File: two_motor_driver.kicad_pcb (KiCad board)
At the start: 4 copper layers, 123.8 x 60 mm, 51 parts, among them M1 Conn_01x03, M2 Conn_01x03, SW1 SW_SPDT, U1 L6234PD, U2 L6234PD, U3 INA181, U4 INA181, U5 my_buck_boost

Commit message: pcb layout
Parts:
- removed .033_1, .033_2: .033, Resistor_SMD:R_1206_3216Metric
- removed .1_1, .1_2: .1, Resistor_SMD:R_1206_3216Metric
- removed .22uF_1, .22uF_2: .22uF, Capacitor_SMD:C_0805_2012Metric
- removed 100nF_1, 100nF_2, C11, C12, C13, C14, C15, C16: 100nF, Capacitor_SMD:C_0805_2012Metric
- removed 100uF_1, 100uF_2: 100uF, Capacitor_SMD:C_1210_3225Metric
- removed 10nF_1, 10nF_2: 10nF, Capacitor_SMD:C_0805_2012Metric
- removed 1uF_1, 1uF_2: 1uF, Capacitor_SMD:C_0805_2012Metric
- removed 90k_1: 90k, Resistor_SMD:R_0805_2012Metric
- removed BJ1: Barrel_Jack, Connector_BarrelJack:BarrelJack_CUI_PJ-063AH_Horizontal
- removed D2, D3: BAT54S, Package_TO_SOT_SMD:SOT-23-3
- removed JP1, JP3, JP4, JP5: SolderJumper_2_Open, Jumper:SolderJumper-2_P1.3mm_Open_TrianglePad1.0x1.5mm
- removed M1, M2, PIR1: Conn_01x03, Connector_PinHeader_2.54mm:PinHeader_1x03_P2.54mm_Vertical
- removed U1, U2: L6234PD, SOIC127P1420X360-21N
- removed U3, U4: INA181, Package_TO_SOT_SMD:SOT-23-6
- added 10k_2: 10k, Resistor_SMD:R_0805_2012Metric, F.Cu at (197.0, 120.4)
- added 90k_2: 90k, Resistor_SMD:R_0805_2012Metric, F.Cu at (197.0, 124.9)
- added C1: 100nF, Capacitor_SMD:C_0805_2012Metric, F.Cu at (198.9, 147.9)
- added C2: 100nF, Capacitor_SMD:C_0805_2012Metric, F.Cu at (201.9, 147.9)
- added FOC1: Conn_01x05, Connector_PinSocket_2.54mm:PinSocket_1x05_P2.54mm_Vertical, F.Cu at (193.4, 95.5)
- added FOC2: Conn_01x05, Connector_PinSocket_2.54mm:PinSocket_1x05_P2.54mm_Vertical, F.Cu at (160.4, 96.0)
- added J1: Conn_01x02, Connector_PinHeader_2.54mm:PinHeader_1x02_P2.54mm_Vertical, F.Cu at (193.0, 107.0)
- added J3: Conn_01x08, Connector_PinSocket_2.54mm:PinSocket_1x08_P2.54mm_Vertical, F.Cu at (155.3, 127.0)
- added POT1: Conn_01x03, Connector_PinHeader_2.54mm:PinHeader_1x03_P2.54mm_Vertical, F.Cu at (140.5, 130.0)
- added RC1: Conn_01x03, Connector_PinHeader_2.54mm:PinHeader_1x03_P2.54mm_Vertical, F.Cu at (180.2, 132.0)
- added RC2: Conn_01x03, Connector_PinHeader_2.54mm:PinHeader_1x03_P2.54mm_Vertical, F.Cu at (184.8, 132.0)
- added RC3: Conn_01x03, Connector_PinHeader_2.54mm:PinHeader_1x03_P2.54mm_Vertical, F.Cu at (189.5, 132.0)
- added SEL1: Conn_01x03, Connector_PinHeader_2.54mm:PinHeader_1x03_P2.54mm_Vertical, F.Cu at (190.0, 125.0)
- added SEL2: Conn_01x03, Connector_PinHeader_2.54mm:PinHeader_1x03_P2.54mm_Vertical, F.Cu at (145.5, 130.0)
- added SEL3: Conn_01x02, Connector_PinHeader_2.54mm:PinHeader_1x02_P2.54mm_Vertical, F.Cu at (190.2, 114.0)
- US5881_1, US5881_2: footprint Sensor_Current:Diodes_SIP-3_4.1x1.5mm_P1.27mm -> Connector_PinHeader_2.54mm:PinHeader_1x03_P2.54mm_Vertical
- moved TP1 65.3 mm to (213.5, 138.5), turned to 0 degrees
- moved U5 60.3 mm to (207.1, 123.3)
- moved US5881_1 53.4 mm to (184.5, 95.5), turned to 0 degrees
- moved SW1 47.8 mm to (201.9, 108.1), turned to 90 degrees
- moved D1 38.0 mm to (196.0, 137.5), turned to 90 degrees
- moved 10k_1 37.7 mm to (179.0, 142.9), turned to 90 degrees
- moved 4.7nF_1 32.3 mm to (192.9, 147.9), turned to 90 degrees
- moved A1 28.5 mm to (180.0, 106.0), turned to -90 degrees
- moved 4.7nF_2 26.1 mm to (195.9, 147.9), turned to 90 degrees
- moved R1 25.9 mm to (186.5, 143.5), turned to 90 degrees
- moved R2 20.9 mm to (189.9, 147.9), turned to 90 degrees
- moved US5881_2 9.79 mm to (180.0, 150.5), turned to 90 degrees
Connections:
- 10k_1 pad 1: Vcc_sense -> BTN1
- A1 pad 1: HS2 -> BTN1
- A1 pad 10: M1_EN -> FOC2_PWM_A
- A1 pad 11: M2_EN -> FOC2_PWM_B
- A1 pad 12: M2_IN1 -> FOC2_PWM_C
- A1 pad 13: M2_IN2 -> /ENC1_A
- A1 pad 14: M2_IN3 -> /ENC1_B
- A1 pad 15: unconnected-(A1-D12/CIPO-Pad15) -> /ENC1_A
- A1 pad 19: unconnected-(A1-A0-Pad19) -> RC_Throttle
- A1 pad 2: HS1 -> /TP1_ESP32
- A1 pad 20: unconnected-(A1-A1-Pad20) -> RC_Mode
- A1 pad 21: unconnected-(A1-A2-Pad21) -> /ENC2_B
- A1 pad 22: SENSE1_1_out -> /HALL_1
- A1 pad 23: SENSE1_2_out -> A4_in
- A1 pad 24: Vcc_sense -> /MPU6050_SCL
- A1 pad 25: unconnected-(A1-A6-Pad25) -> /HALL_2
- A1 pad 26: unconnected-(A1-A7-Pad26) -> A7_in
- A1 pad 27: unconnected-(A1-VUSB/5V-Pad27) -> +5V
- A1 pad 5: unconnected-(A1-D2-Pad5) -> FOC1_EN
- A1 pad 6: M1_IN1 -> FOC1_PWM_A
- A1 pad 7: PIR -> FOC1_PWM_B
- A1 pad 8: M1_IN2 -> FOC1_PWM_C
- A1 pad 9: M1_IN3 -> FOC2_EN
- D1 pad 1: Vcc -> GND
- D1 pad 2: VBOOT1 -> +3.3V
- U5 pad 7: +3.3V -> +5V
- U5 pad 8: +3.3V -> +5V
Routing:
- net Vcc: track 231.6 -> 0.00 mm, vias 6 -> 0
- net M2_EN: track 93.8 -> 0.00 mm, vias 4 -> 0
- net M2_IN3: track 75.9 -> 0.00 mm
- net M2_IN2: track 56.6 -> 0.00 mm, vias 2 -> 0
- net M2_IN1: track 50.1 -> 0.00 mm
- net M1_EN: track 44.5 -> 0.00 mm, vias 3 -> 0
- net SENSE1_2_out: track 42.1 -> 0.00 mm, vias 3 -> 0
- net SENSE1_1_out: track 40.8 -> 0.00 mm, vias 1 -> 0
- net HS1: track 34.6 -> 0.00 mm, vias 1 -> 0
- net M1_IN1: track 34.0 -> 0.00 mm, vias 1 -> 0
- net Vcc_sense: track 33.3 -> 0.00 mm
- net M1_IN3: track 33.3 -> 0.00 mm, vias 2 -> 0
- net M1_IN2: track 31.5 -> 0.00 mm, vias 1 -> 0
- net HS2: track 25.4 -> 0.00 mm, vias 1 -> 0
- net GND: track 22.1 -> 0.00 mm, vias 55 -> 0
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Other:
- board size 123.8 x 60 mm -> 78 x 60 mm
- board text added: "FOC_NANO_V1.0"
- board text removed: "+"
- board text removed: "+3.3V"
- board text removed: ".033"
- board text removed: "0.1"
- board text removed: "Be sure to select solder"
- board text removed: "GND"
- board text removed: "M1"
- board text removed: "M2"
- board text removed: "Vcc"
- board text removed: "arduino nano esp32"
- board text removed: "bridges before testing"
- board text removed: "two motor V1.0"
- board text removed: "unswitched"

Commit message: started layout
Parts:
- removed the 10k_1 at (179.0, 142.9)
- removed A1: Arduino_Nano_ESP32, Module:Arduino_Nano
- removed POT1, SEL1, SEL2, TP1: Conn_01x03, Connector_PinHeader_2.54mm:PinHeader_1x03_P2.54mm_Vertical
- removed SEL3: Conn_01x02, Connector_PinHeader_2.54mm:PinHeader_1x02_P2.54mm_Vertical
- added 10k_2: 10k, Resistor_SMD:R_0805_2012Metric, F.Cu at (181.6, 131.5)
- added ENC1: J1, Connector_PinSocket_2.54mm:PinSocket_1x04_P2.54mm_Vertical, F.Cu at (125.0, 103.2)
- added ENC2: J1, Connector_PinSocket_2.54mm:PinSocket_1x04_P2.54mm_Vertical, F.Cu at (125.0, 126.9)
- added J2: ESP PROG, Connector_PinSocket_2.54mm:PinSocket_1x04_P2.54mm_Vertical, F.Cu at (180.4, 113.8)
- added J5: Conn_01x01, Connector_PinSocket_2.54mm:PinSocket_1x01_P2.54mm_Vertical, F.Cu at (213.5, 138.5)
- added J6: Conn_01x01, Connector_PinSocket_2.54mm:PinSocket_1x01_P2.54mm_Vertical, F.Cu at (199.5, 139.0)
- added J7: Conn_01x01, Connector_PinSocket_2.54mm:PinSocket_1x01_P2.54mm_Vertical, F.Cu at (204.5, 150.0)
- added LS1: Speaker, CDS-13138-SMT-TR:SPKR_CDS-13138-SMT-TR, F.Cu at (135.8, 139.2)
- added M1: Conn_01x02, Connector_PinHeader_2.54mm:PinHeader_1x02_P2.54mm_Vertical, F.Cu at (124.5, 117.8)
- added M2: Conn_01x02, Connector_PinHeader_2.54mm:PinHeader_1x02_P2.54mm_Vertical, F.Cu at (124.5, 143.5)
- added SW2: SW_Push, Button_Switch_SMD:SW_Push_SPST_NO_Alps_SKRK, F.Cu at (188.1, 140.5)
- added U1: Teensy4.0, simpleFOC_board:Teensy40, F.Cu at (139.4, 112.5)
- added U2: ESP32-C3-DevKitM-1, RF_Module:ESP32-C3-DevKitM-1, F.Cu at (152.1, 95.0)
- moved FOC1 74.9 mm to (118.5, 95.8), turned to 0 degrees
- moved FOC2 51.7 mm to (118.5, 126.2), turned to 0 degrees
- moved C1 38.6 mm to (186.7, 111.2), turned to -90 degrees
- moved 4.7nF_1 36.7 mm to (193.7, 111.2), turned to 0 degrees
- moved 10k_3 35.8 mm to (192.9, 108.2), turned to -90 degrees
- moved RC3 35.8 mm to (196.9, 97.0)
- moved RC2 35.5 mm to (190.4, 97.0)
- moved RC1 35.2 mm to (183.9, 97.0)
- moved US5881_2 32.7 mm to (189.7, 119.3), turned to 0 degrees
- moved C2 29.8 mm to (186.7, 122.2), turned to -90 degrees
- moved 10k_4 28.3 mm to (192.9, 119.8), turned to -90 degrees
- moved 4.7nF_2 25.2 mm to (193.7, 122.8), turned to 0 degrees
- moved J3 24.6 mm to (146.6, 150.0), turned to -90 degrees
- moved REF** 23.3 mm to (118.5, 149.2)
- moved REF** 16.3 mm to (125.5, 97.0)
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- renumbered 10k_2 to 10k_1, R1 to 10k_3, R2 to 10k_4, 90k_2 to 90k_1
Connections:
- net HS1 renamed HALL_1
- net HS2 renamed HALL_2
- net Net-(SEL1-Pin_3) renamed /VSense_in
- J3 pad 4: MPU6050_SDA -> /MPU6050_SDA
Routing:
- net RC_Mode: track 0.00 -> 73.4 mm
- net +5V: track 0.00 -> 54.2 mm
- net RC_Steering: track 0.00 -> 51.5 mm, vias 0 -> 1
- net /ESP32_MOSI: track 0.00 -> 49.5 mm
- net RC_Throttle: track 0.00 -> 46.7 mm, vias 0 -> 1
- net /ESP32_MISO: track 0.00 -> 36.8 mm
- net /ESP32_CLK: track 0.00 -> 35.1 mm
- net /ENC2_B: track 0.00 -> 26.4 mm
- net /ENC2_A: track 0.00 -> 25.6 mm
- net /ESP32_CS: track 0.00 -> 22.8 mm
- net HALL_1: track 0.00 -> 22.6 mm
- net FOC1_PWM_A: track 0.00 -> 22.3 mm
- net HALL_2: track 0.00 -> 21.5 mm
- net FOC2_PWM_A: track 0.00 -> 21.2 mm
- net FOC2_PWM_B: track 0.00 -> 20.2 mm
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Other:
- board size 78 x 60 mm -> 101 x 60.3 mm
- board text added: "+5V"
- board text added: "3.3V"
- board text added: "ESP PROG"
- board text added: "GND"
- board text added: "Vcc"

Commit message: completing traces
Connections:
- U2 pad 13: unconnected-(U2-5V-Pad13) -> +5V
- U2 pad 14: unconnected-(U2-5V-Pad13)_1 -> +5V
- U2 pad 2: +3.3V -> unconnected-(U2-3V3-Pad2)
- U2 pad 3: +3.3V -> unconnected-(U2-3V3-Pad2)_1
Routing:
- net Vcc: track 0.00 -> 204.3 mm
- net +5V: track 54.2 -> 156.2 mm
- net BTN1: track 0.00 -> 69.7 mm, vias 0 -> 1
- net /VSense_in: track 0.00 -> 53.1 mm
- net /MPU6050_SCL: track 0.00 -> 39.8 mm, vias 0 -> 1
- net /MPU6050_SDA: track 0.00 -> 39.2 mm, vias 0 -> 1
- net /SPEAKER: track 0.00 -> 38.6 mm, vias 0 -> 1
- net Net-(J1-Pin_2): track 0.00 -> 12.3 mm
- net +3.3V: track 10.8 -> 22.3 mm, vias 2 -> 3
- net RC_Mode: track 73.4 -> 68.9 mm
- net /ESP32_CLK: track 35.1 -> 37.0 mm
- net /ENC2_A: track 25.6 -> 26.3 mm
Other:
- board text added: "FOC_TEENSY_V1.0"
- board text removed: "FOC_NANO_V1.0"

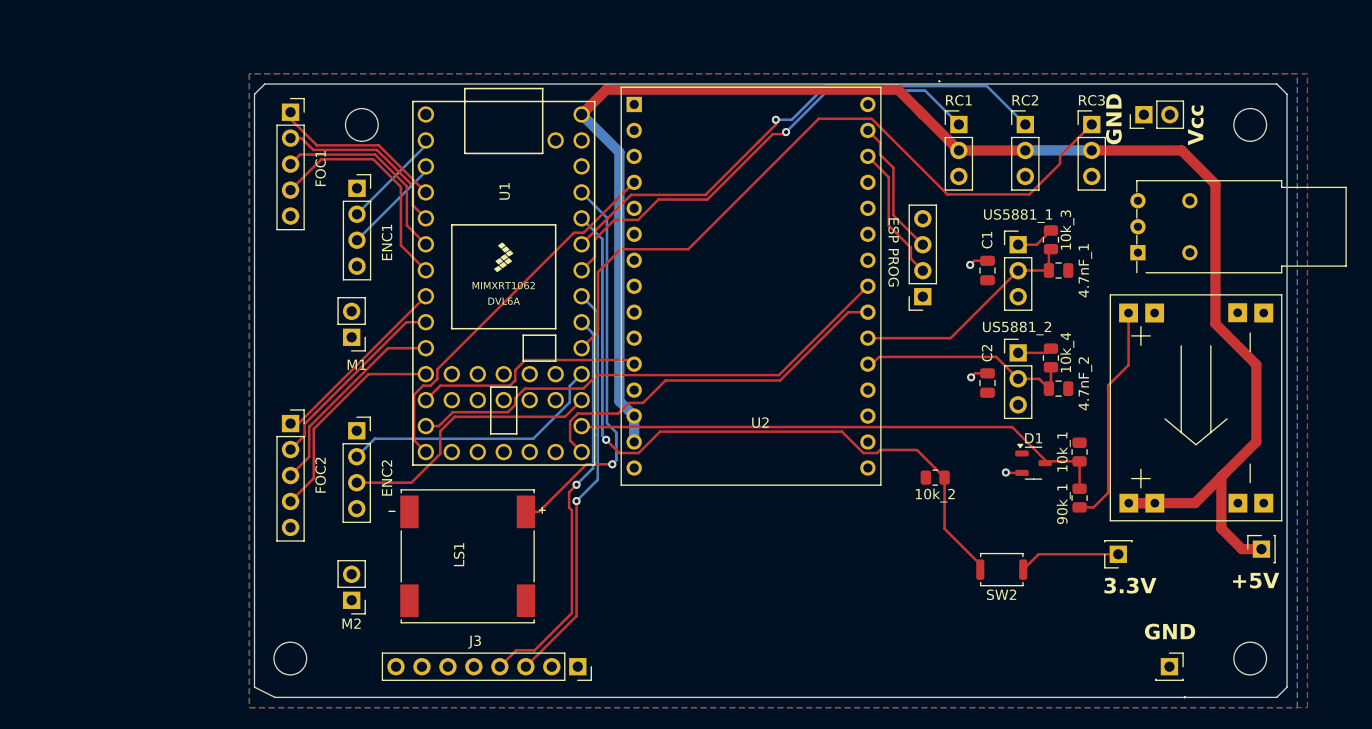
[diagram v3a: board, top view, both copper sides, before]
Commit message: added DRV8313
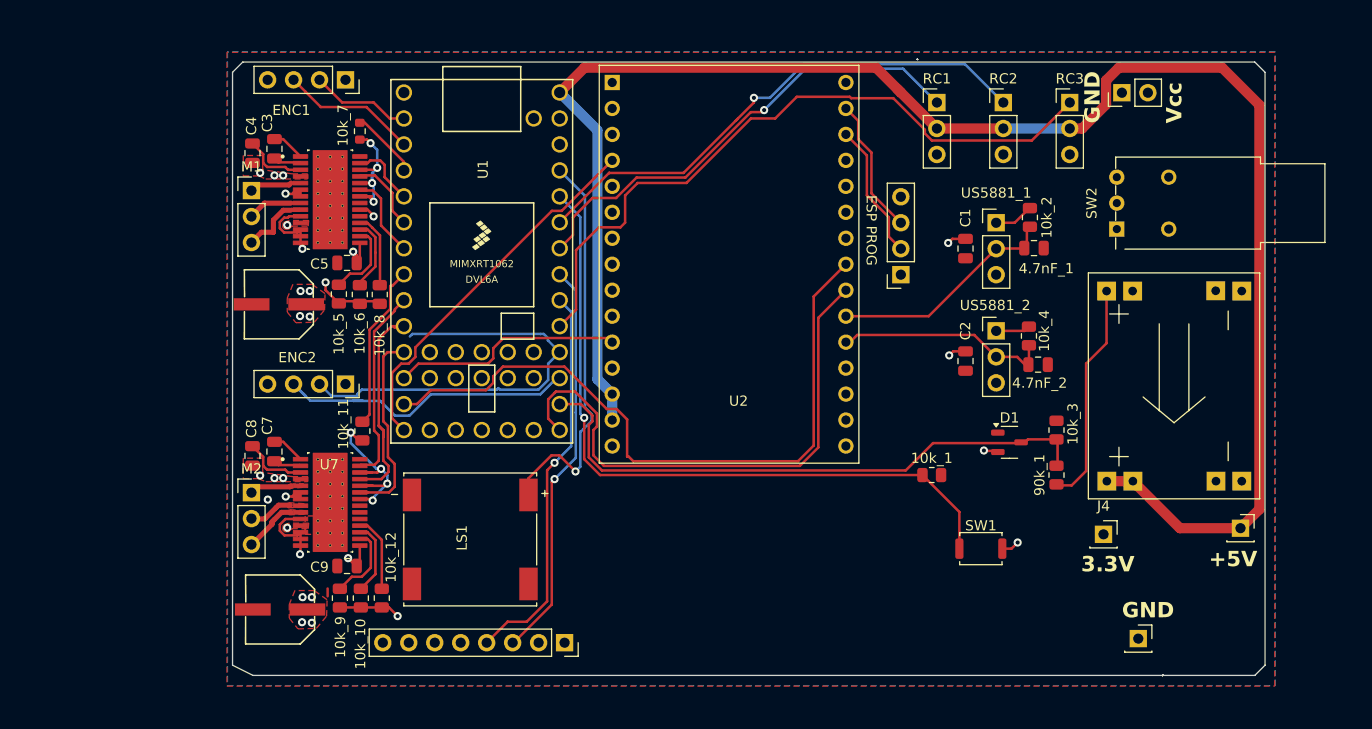
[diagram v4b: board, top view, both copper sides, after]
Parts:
- removed FOC1, FOC2: Conn_01x05, Connector_PinSocket_2.54mm:PinSocket_1x05_P2.54mm_Vertical
- removed J7: Conn_01x01, Connector_PinSocket_2.54mm:PinSocket_1x01_P2.54mm_Vertical
- removed REF** (x4): MountingHole_3.2mm_M3, MountingHole:MountingHole_3.2mm_M3
- added 10k_10: 10k, Resistor_SMD:R_0805_2012Metric, F.Cu at (125.4, 143.3)
- added 10k_11: 10k, Resistor_SMD:R_0805_2012Metric, F.Cu at (125.5, 127.0)
- added 10k_12: 10k, Resistor_SMD:R_0805_2012Metric, F.Cu at (127.5, 143.3)
- added 10k_5: 10k, Resistor_SMD:R_0805_2012Metric, F.Cu at (123.2, 113.5)
- added 10k_6: 10k, Resistor_SMD:R_0805_2012Metric, F.Cu at (125.3, 113.6)
- added 10k_7: 10k, Resistor_SMD:R_0603_1608Metric, F.Cu at (125.3, 97.6)
- added 10k_8: 10k, Resistor_SMD:R_0805_2012Metric, F.Cu at (127.2, 113.6)
- added 10k_9: 10k, Resistor_SMD:R_0805_2012Metric, F.Cu at (123.3, 143.3)
- added C10: C_Polarized_Small, Capacitor_SMD:CAP-SMD_BD6.3-L6.6-W6.6-FD, F.Cu at (117.5, 144.4)
- added C3: 100nF, Capacitor_SMD:C_0805_2012Metric, F.Cu at (117.0, 99.3)
- added C4: 100nF, Capacitor_SMD:C_0805_2012Metric, F.Cu at (114.8, 99.8)
- added C5: 470nF, Capacitor_SMD:C_0805_2012Metric, F.Cu at (124.0, 110.5)
- added C6: C_Polarized_Small, Capacitor_SMD:CAP-SMD_BD6.3-L6.6-W6.6-FD, F.Cu at (117.4, 114.5)
- added C7: 100nF, Capacitor_SMD:C_0805_2012Metric, F.Cu at (117.0, 128.9)
- added C8: 100nF, Capacitor_SMD:C_0805_2012Metric, F.Cu at (114.8, 129.4)
- added C9: 470nF, Capacitor_SMD:C_0805_2012Metric, F.Cu at (124.0, 140.2)
- added J4: Conn_01x01, Connector_PinSocket_2.54mm:PinSocket_1x01_P2.54mm_Vertical, F.Cu at (198.1, 137.1)
- added U6: DRV8313PWP, DRV8313PWP:SOP65P640X120-29N, F.Cu at (122.4, 104.3)
- added U7: DRV8313PWP, DRV8313PWP:SOP65P640X120-29N, F.Cu at (122.4, 133.9)
- J3: value Conn_01x08 -> Conn_01x01; footprint Connector_PinSocket_2.54mm:PinSocket_1x08_P2.54mm_Vertical -> Connector_PinSocket_2.54mm:PinSocket_1x01_P2.54mm_Vertical
- J6: value Conn_01x01 -> Conn_01x08; footprint Connector_PinSocket_2.54mm:PinSocket_1x01_P2.54mm_Vertical -> Connector_PinSocket_2.54mm:PinSocket_1x08_P2.54mm_Vertical
- M1, M2: value Conn_01x02 -> Conn_01x03; footprint Connector_PinHeader_2.54mm:PinHeader_1x02_P2.54mm_Vertical -> Connector_PinHeader_2.54mm:PinHeader_1x03_P2.54mm_Vertical
- SW1: value SW_SPDT -> SW_Push; footprint Button_Switch_THT:SW_NKK_BB15AH -> Button_Switch_SMD:SW_Push_SPST_NO_Alps_SKRK
- SW2: value SW_Push -> SW_SPDT; footprint Button_Switch_SMD:SW_Push_SPST_NO_Alps_SKRK -> Button_Switch_THT:SW_NKK_BB15AH
- moved J3 66.2 mm to (211.4, 136.4), turned to 0 degrees
- moved J6 54.9 mm to (145.3, 147.7), turned to -90 degrees
- moved SW2 35.2 mm to (199.3, 107.2), turned to 90 degrees
- moved SW1 32.8 mm to (186.1, 138.4), turned to 0 degrees
- moved 10k_2 27.1 mm to (190.8, 106.0), turned to -90 degrees
- moved 10k_3 18.6 mm to (193.4, 126.8), turned to 90 degrees
- moved M1 17.4 mm to (114.7, 103.4), turned to 0 degrees
- moved J5 14.9 mm to (201.4, 147.2), turned to 0 degrees
- moved 10k_1 14.6 mm to (181.2, 131.2), turned to 0 degrees
- moved M2 14.4 mm to (114.7, 133.0), turned to 0 degrees
- moved ENC1 10.7 mm to (123.9, 92.6), turned to -90 degrees
- moved ENC2 4.70 mm to (123.9, 122.3), turned to -90 degrees
- moved 4.7nF_1 3.25 mm to (191.2, 109.0)
- moved 90k_1 3.19 mm to (193.4, 131.2)
- moved D1 3.12 mm to (188.8, 128.1)
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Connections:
- net /ENC1_A renamed /teensy/ENC1_A
- net /ENC1_B renamed /teensy/ENC1_B
- net /ENC2_A renamed /teensy/ENC2_A
- net /ENC2_B renamed /teensy/ENC2_B
- net /ESP32_CLK renamed /teensy/ESP32_CLK
- net /ESP32_CS renamed /teensy/ESP32_CS
- net /ESP32_MISO renamed /teensy/ESP32_MISO
- net /ESP32_MOSI renamed /teensy/ESP32_MOSI
- net /ESP32_RX renamed /teensy/ESP32_RX
- net /ESP32_TX renamed /teensy/ESP32_TX
- net /SPEAKER renamed /teensy/SPEAKER
- 10k_1 pad 1: /VSense_in -> BTN1
- 10k_2 pad 1: BTN1 -> +3.3V
- 10k_2 pad 2: GND -> HALL_1
- 10k_3 pad 1: +3.3V -> /teensy/VSense_in
- 10k_3 pad 2: HALL_1 -> GND
- 90k_1 pad 2: /VSense_in -> /teensy/VSense_in
- D1 pad 3: /VSense_in -> /teensy/VSense_in
- J3 pad 1: +3.3V -> +5V
- J5 pad 1: +5V -> GND
- M1 pad 1: Vcc -> Net-(M1-Pin_1)
- M1 pad 2: GND -> Net-(M1-Pin_2)
- M2 pad 1: Vcc -> Net-(M2-Pin_1)
- M2 pad 2: GND -> Net-(M2-Pin_2)
- SW1 pad 1: Vcc -> BTN1
- SW1 pad 2: Net-(J1-Pin_2) -> +3.3V
- SW2 pad 1: BTN1 -> Vcc
- SW2 pad 2: +3.3V -> Net-(J1-Pin_2)
- U1 pad 11: FOC2_PWM_A -> FOC2_PWM_C
- U1 pad 21: /VSense_in -> /teensy/VSense_in
- U1 pad 25: /MPU6050_SDA -> /teensy/MPU6050_SDA
- U1 pad 26: /MPU6050_SCL -> /teensy/MPU6050_SCL
- U1 pad 5: FOC1_PWM_C -> FOC1_PWM_A
- U1 pad 7: FOC1_PWM_A -> FOC1_PWM_C
- U1 pad 9: FOC2_PWM_C -> FOC2_PWM_A
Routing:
- net /teensy/VSense_in: track 0.00 -> 58.2 mm
- net /VSense_in: track 53.1 -> 0.00 mm
- net /MPU6050_SCL: track 39.8 -> 0.00 mm, vias 1 -> 0
- net /teensy/MPU6050_SCL: track 0.00 -> 39.3 mm, vias 0 -> 1
- net /MPU6050_SDA: track 39.2 -> 0.00 mm, vias 1 -> 0
- net /teensy/MPU6050_SDA: track 0.00 -> 38.5 mm, vias 0 -> 1
- net Vcc: track 204.3 -> 232.0 mm, vias 0 -> 16
- net GND: track 0.00 -> 24.0 mm, vias 0 -> 6
- net Net-(U7-EN1): track 0.00 -> 19.2 mm, vias 0 -> 4
- net /teensy/ESP32_MOSI: track 49.3 -> 67.6 mm
- net /teensy/ESP32_CLK: track 37.0 -> 53.4 mm
- net /teensy/ENC2_A: track 26.3 -> 42.5 mm
- net FOC1_PWM_A: track 22.3 -> 6.58 mm
- net Net-(U6-EN1): track 0.00 -> 14.1 mm, vias 0 -> 4
- net +5V: track 156.2 -> 169.2 mm
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- added copper zone on F.Cu, net Net-(M2-Pin_1)
- added copper zone on F.Cu, net Net-(M2-Pin_2)
- added copper zone on F.Cu, net Net-(M2-Pin_3)
- added copper zone on F.Cu, net Vcc
